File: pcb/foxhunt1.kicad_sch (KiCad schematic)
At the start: 0 parts

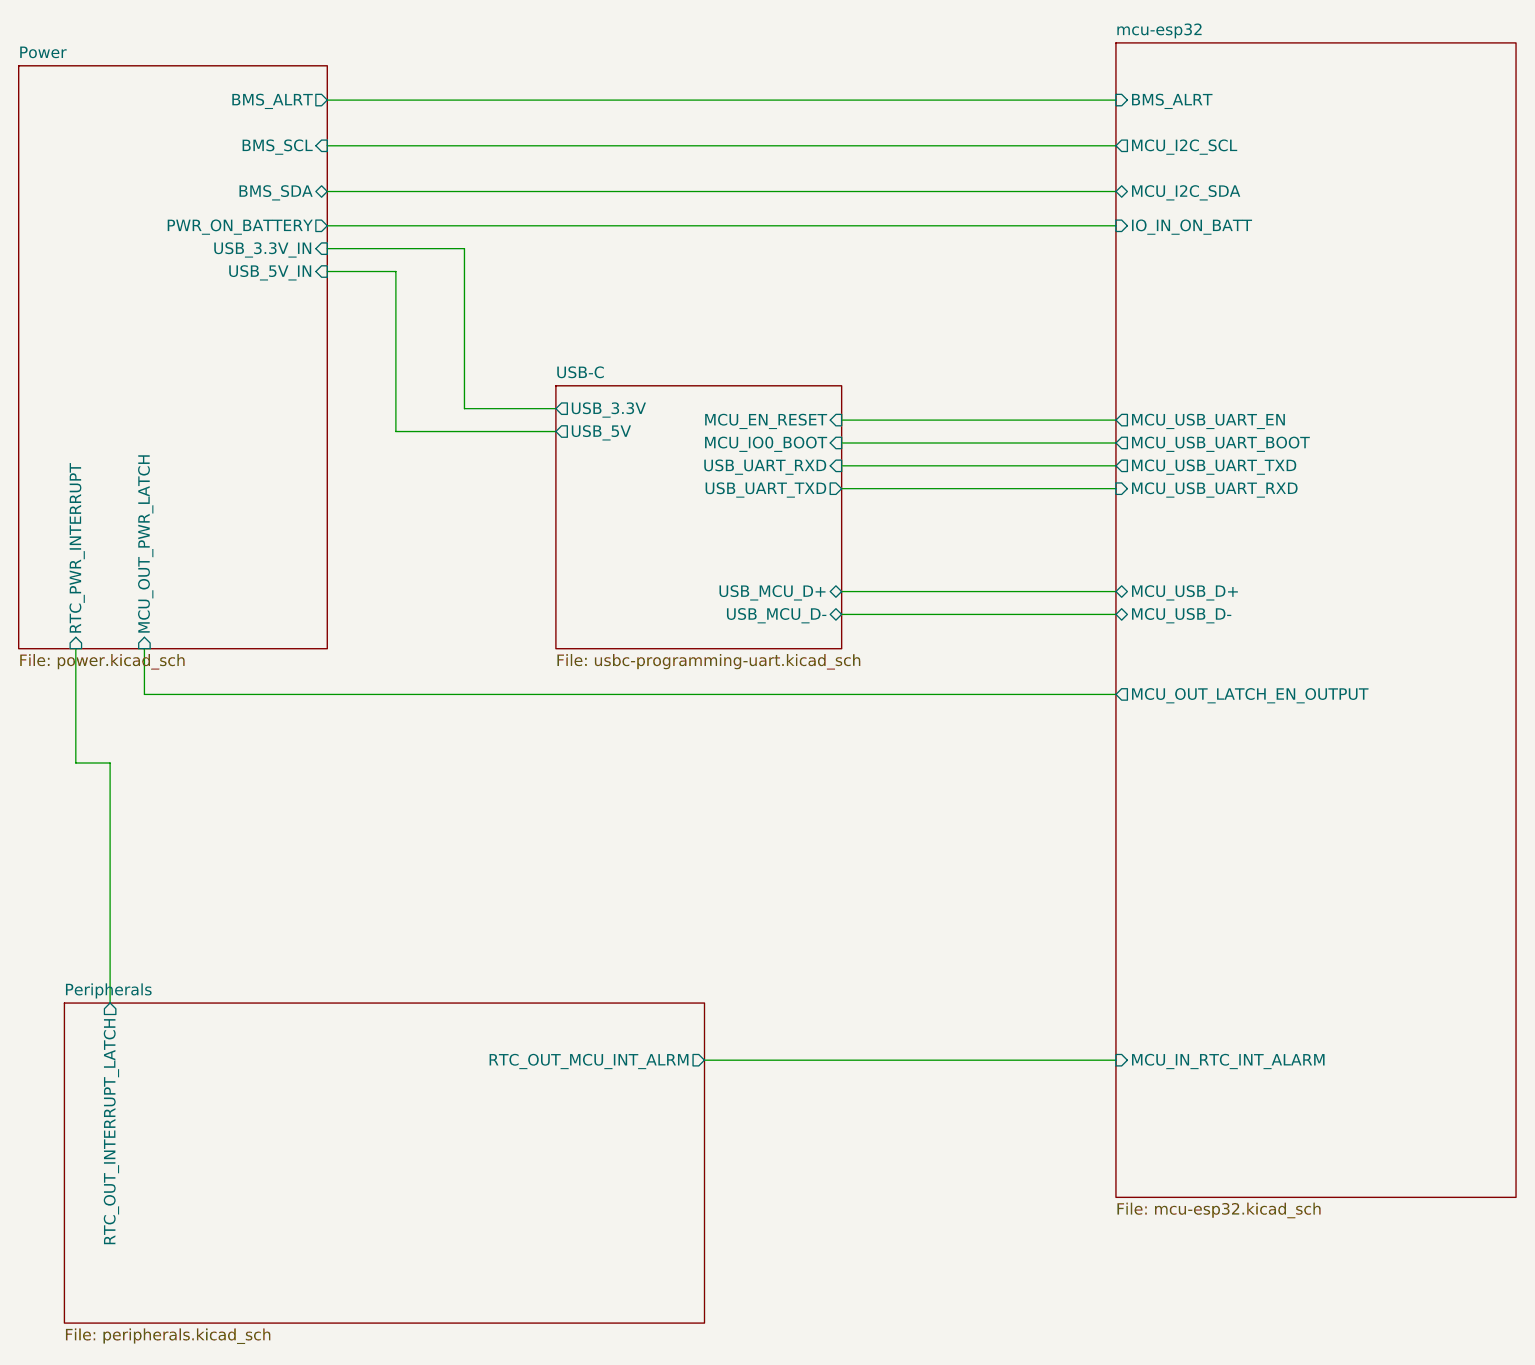
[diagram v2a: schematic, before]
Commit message: Build out PCF8563 RTC peripheral circuit and wire into VRAW latch/MCU
- U14 (PCF8563T) with NDK 9pF crystal (Y2) and DNP OSCI trim cap (C43)
- Coin-cell backup diode-OR: D2/D3 (BAS116) commoned into VDD, BT3
  (CR2032) as backup source, main 3.3V rail as primary
- INT -> Q8 (AO3407A, 3.3V-domain inverter) -> Q7 (BSS138, voltage-safe
  level shift) -> RTC_OUT_INTERRUPT_LATCH, with R31 gate pull-down so
  Q7 has a defined off-state; preserves active-low assert sense onto
  the shared VRAW latch wake node
- R32/R33 (10k) I2C pull-ups on the shared SDA/SCL bus (mcu-esp32,
  Peripherals, and the fuel gauge on Power all share one bus/pull-up
  pair)
- Bump kicad_gx_library for the vendored BAS116LT1G symbol/footprint

Co-Authored-By: Claude Sonnet 5 <noreply@anthropic.com>
Claude-Session: https://claude.ai/code/session_01LhLkuH6sQ5GbUZ61bG7p2h
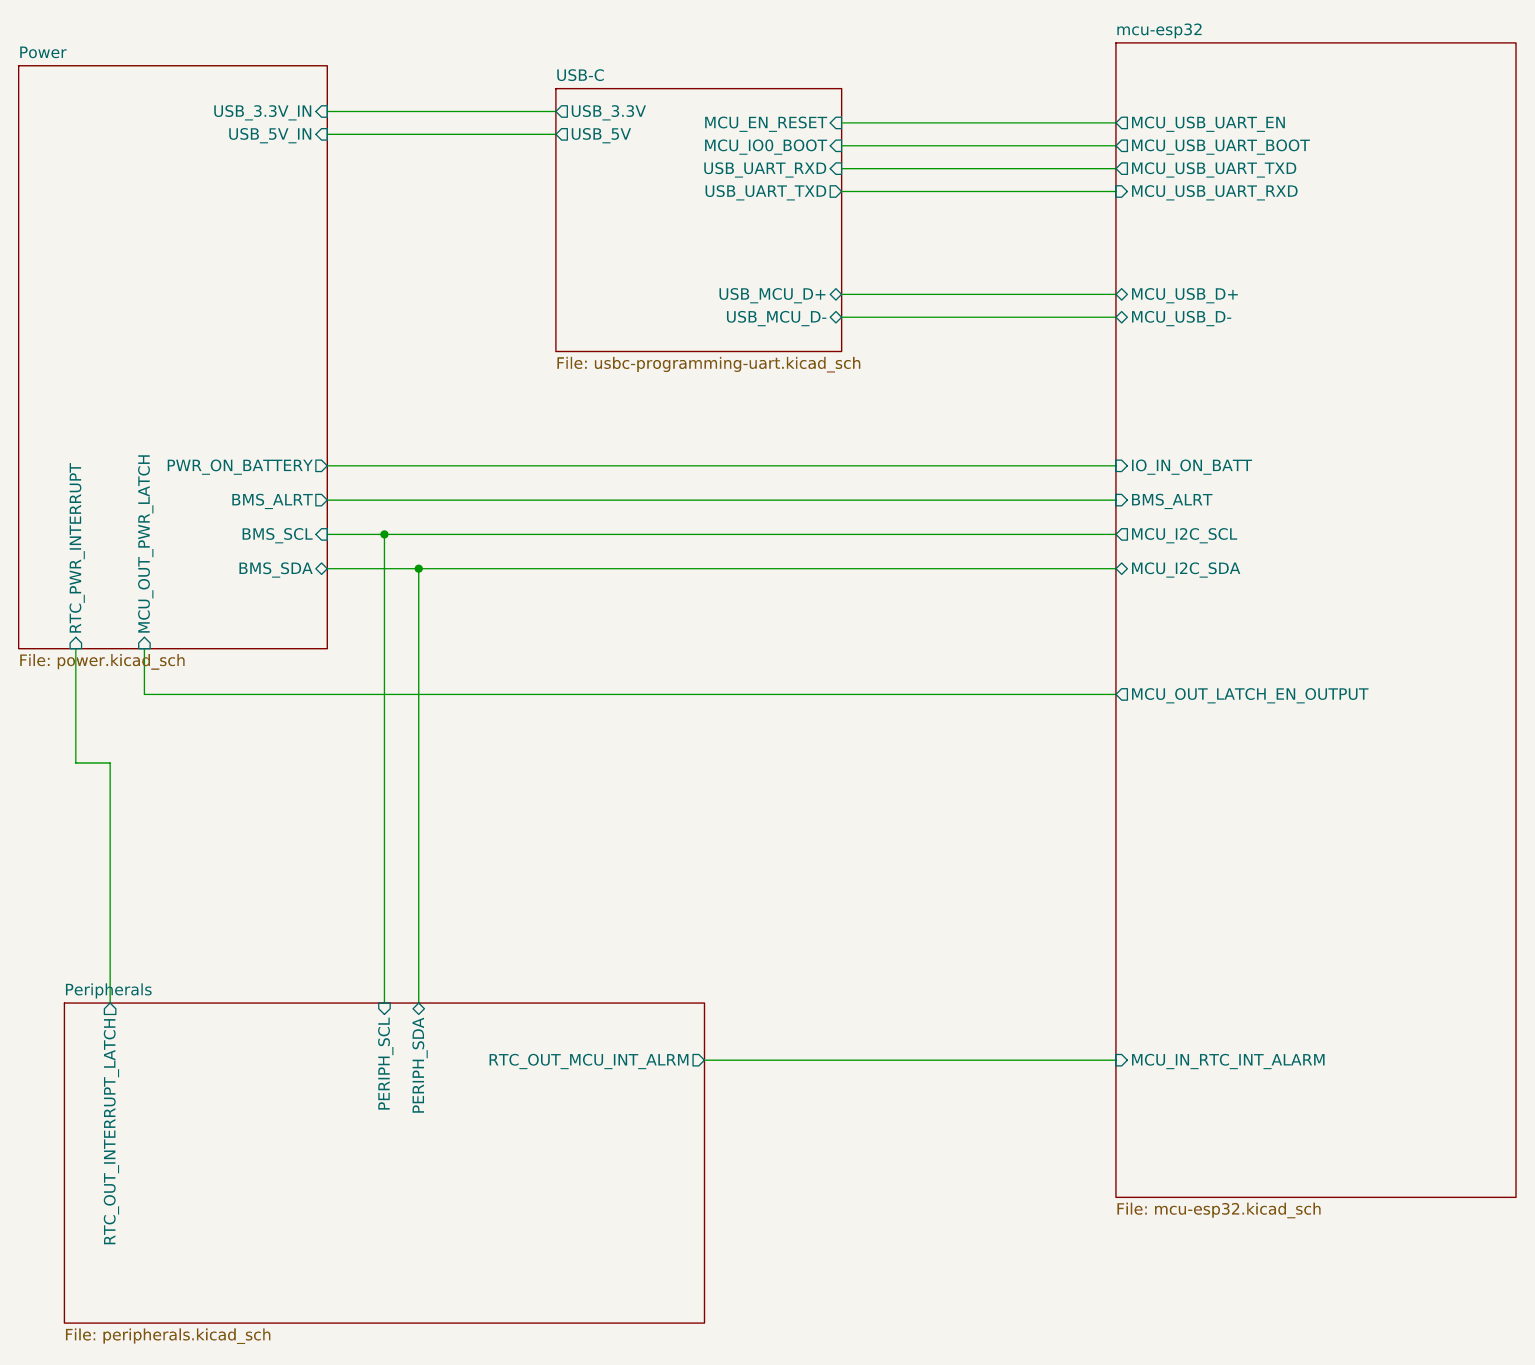
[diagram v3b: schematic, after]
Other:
- sheet Peripherals ports: added PERIPH_SCL, PERIPH_SDA; removed none

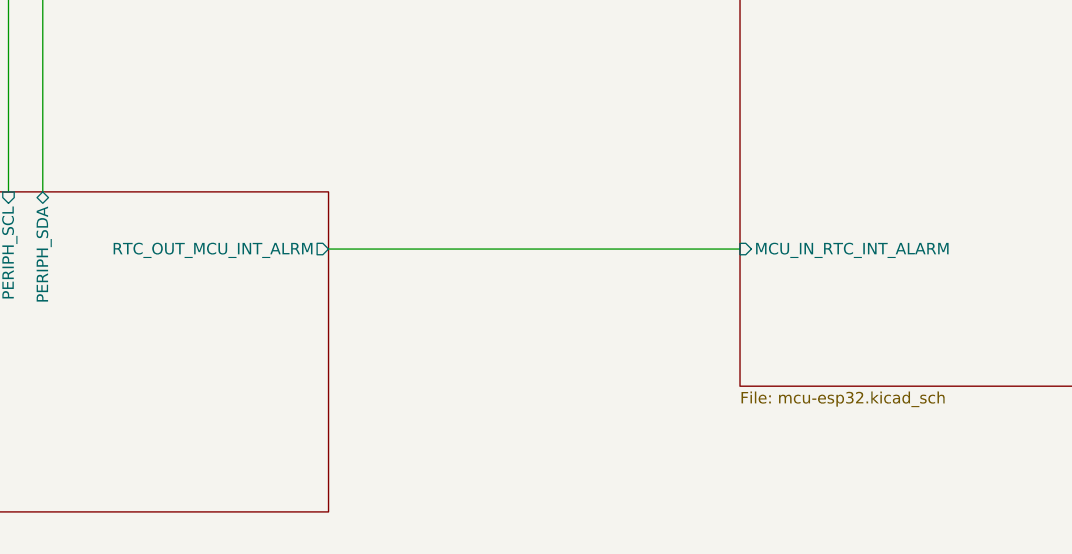
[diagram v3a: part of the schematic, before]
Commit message: Wire up PCA9555 expansion IO section, source LEDs/resistors, swap 3.3V LDO to LM1117
- PCA9555PW expansion IO: DIP switch (SW4, IO0_0-3), onboard buttons
  (SW7-10), status LEDs (D7-10) with sourced series resistors, external
  JST breakouts (J4-7/R39-42) for IO0_4-7, INT pull-up (R34), VDD bypass
  (C49), address pins grounded (addr 0x20)
- Route PCA9555 INT (PERIPH_IO_INT) across the Power/mcu-esp32 top-level
  sheets to the ESP32-S3 (MCU_IN_IO_INT)
- Source real YAGEO MPN/LCSC part numbers for R30/R31/R34-R42
- Fix D10 LED (was orange 0603 with an LCSC part# that resolved to a
  different, wrong part) -> yellow 0805 APTD2012LSYCK, verified Vf/LCSC
  match, matching D7-9's package family
- Fix stale copy-pasted Datasheet links on D7-9 and R31/R35
- Swap 3.3V LDO from AMS1117-3.3 to TI LM1117IMPX-3.3/NOPB (5V LDO swap
  from LM1085IS-5.0 still pending)

Co-Authored-By: Claude Sonnet 5 <noreply@anthropic.com>
Claude-Session: https://claude.ai/code/session_01LhLkuH6sQ5GbUZ61bG7p2h
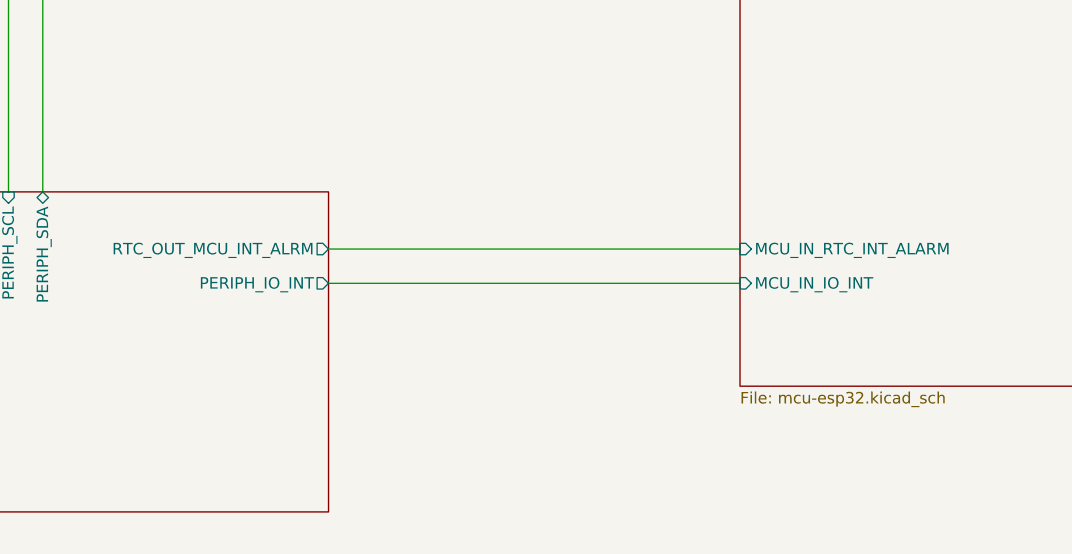
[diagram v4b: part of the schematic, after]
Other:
- sheet Peripherals ports: added PERIPH_IO_INT; removed none
- sheet mcu-esp32 ports: added MCU_IN_IO_INT; removed none
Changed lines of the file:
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@@
+	(wire
+		(pts
+			(xy 120.65 149.86) (xy 166.37 149.86)
+		)
+		(stroke
+			(width 0)
+			(type default)
+		)
+	)
 	(wire
 		(pts
@@
 			)
 		)
+		(pin "MCU_IN_IO_INT" input
+			(at 166.37 149.86 180)
+			(effects
+				(font
+					(size 1.27 1.27)
+				)
+				(justify left)
+			)
+		)
 		(instances
 			(project "foxhunt1"
@@
 			(effects
 				(font
+					(size 1.27 1.27)
+				)
+				(justify right)
+			)
+		)
+		(pin "PERIPH_IO_INT" output
+			(at 120.65 149.86 0)
+			(effects
+				(font
